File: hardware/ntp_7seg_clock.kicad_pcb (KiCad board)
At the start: 2 copper layers, 61 x 33 mm, 43 parts, among them J1 Barrel_Jack, J2 Conn_02x04_Odd_Even, J3 Conn_02x04_Odd_Even, J4 Conn_02x04_Odd_Even, J5 Conn_02x04_Odd_Even, J6 Conn_01x06_Male, Q1 NJL7302L-F3, Q2 Q_NPN_BEC, Q3 Q_NPN_BEC, SW1 SW_PUSH_SMALL_H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

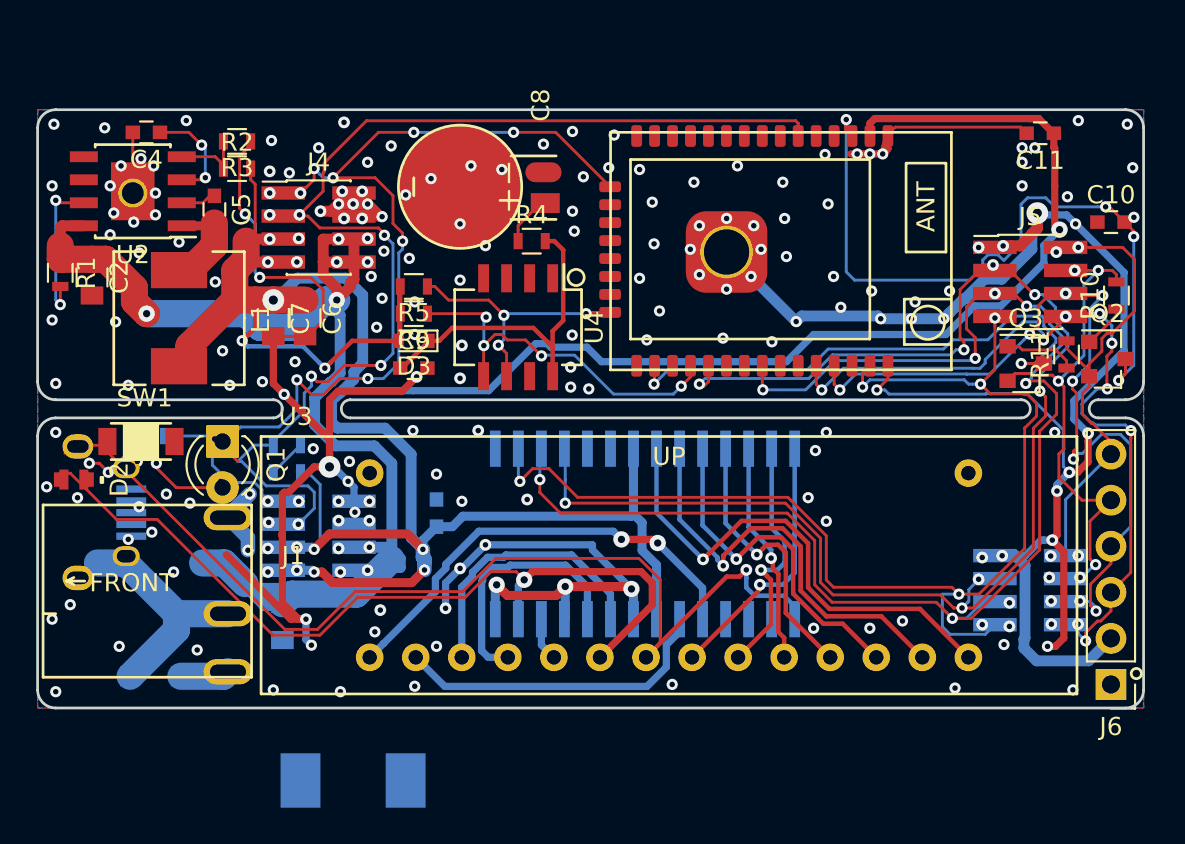
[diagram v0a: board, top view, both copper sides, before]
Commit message: Improved RTC 3V3 backup voltage handling
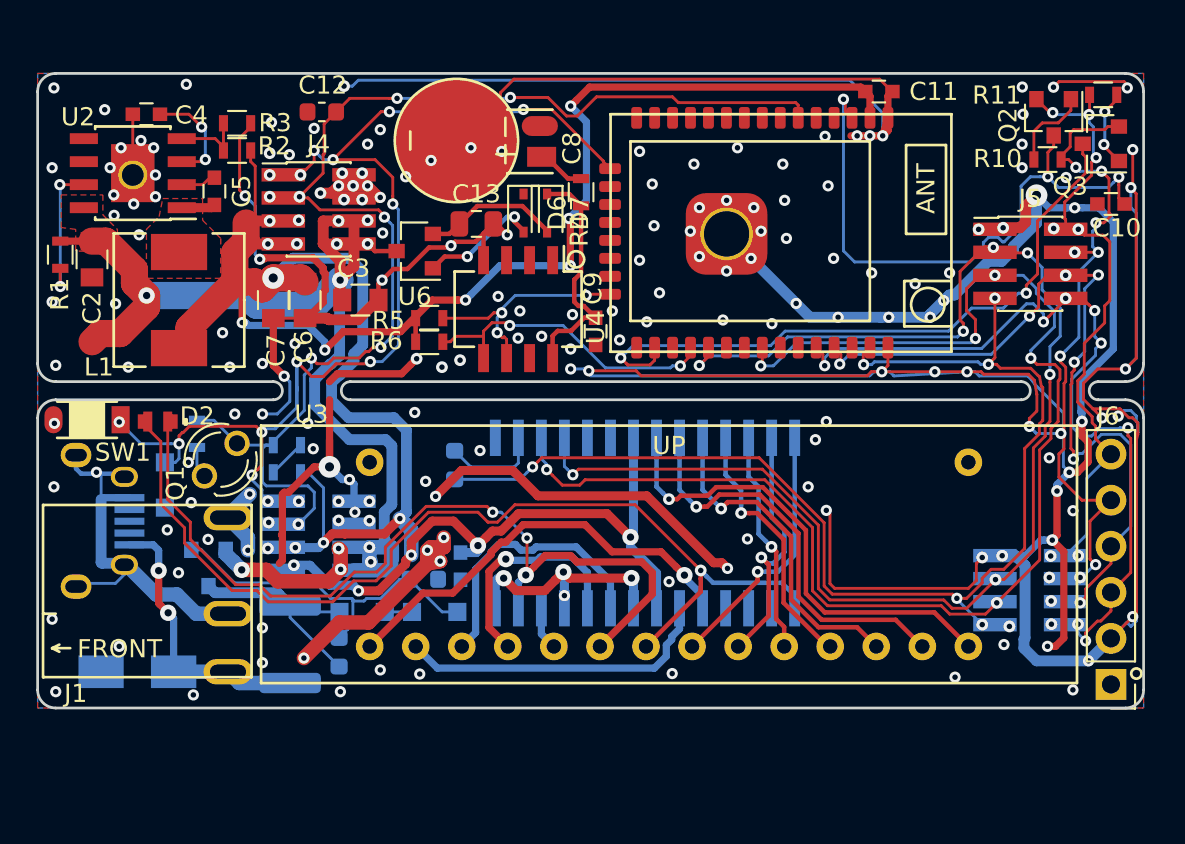
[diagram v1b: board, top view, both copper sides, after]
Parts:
- removed REF**: USB_Micro-B_Jing_A01SB141B1-067, components:USB_Micro-B_Jing_A01SB141B1-067
- added C12: 2.2u, Capacitor_SMD:C_0603_1608Metric, F.Cu at (155.7, 33.1)
- added C13: 10u/35V, Capacitor_SMD:C_0805_2012Metric, F.Cu at (164.2, 39.3)
- added D4: ESD5Z3.3T1G, Diode_SMD:D_SOD-323_HandSoldering, B.Cu at (147.0, 53.7)
- added D5: ESD5Z3.3T1G, Diode_SMD:D_SOD-323_HandSoldering, B.Cu at (157.9, 60.7)
- added D6: 1N4148W, Diode_SMD:D_SOD-323, F.Cu at (166.8, 38.7)
- added D7: 1N4148W, Diode_SMD:D_SOD-323, F.Cu at (168.1, 38.7)
- added J7: USB_B_Micro, components:USB_Micro-B_Jing_A01SB141B1-067, B.Cu at (144.8, 55.7)
- added Q4: AO3401, Package_TO_SOT_SMD:SOT-23, B.Cu at (149.4, 58.3)
- added R12: 1M, Resistor_SMD:R_0603_1608Metric, B.Cu at (156.6, 62.9)
- added R13: 22K, Resistor_SMD:R_0603_1608Metric, B.Cu at (161.3, 58.9)
- added R14: 120R, Resistor_SMD:R_0603_1608Metric, B.Cu at (163.0, 52.6)
- added U6: SE8533X2-HF, Package_TO_SOT_SMD:SOT-23, F.Cu at (160.8, 40.8)
- C3: moved to F.Cu
- D1: value D_Zener_Small -> 28V TVS; footprint Diodes_SMD:D_SOD-123F -> Diode_SMD:D_SMA
- D3: value SBD 40V 200mA -> ESD5Z3.3T1G; footprint Diodes_SMD:D_0603 -> Diode_SMD:D_SOD-323_HandSoldering; moved to B.Cu
- F1: value Polyfuse_Small -> 1A hold; footprint Capacitors_SMD:C_1812_HandSoldering -> Fuse:Fuse_1812_4532Metric
- R4: value 10R -> 1k
- moved C3 18.3 mm to (157.8, 43.5), turned to 0 degrees
- moved D3 15.0 mm to (161.9, 60.7), turned to 0 degrees
- moved R11 14.5 mm to (198.8, 32.2), turned to 180 degrees
- moved Q2 13.7 mm to (196.0, 33.4), turned to 270 degrees
- moved Q3 12.8 mm to (198.6, 34.9), turned to 180 degrees
- moved C9 10.2 mm to (170.8, 45.2), turned to 270 degrees
- moved C11 9.19 mm to (186.4, 32.0), turned to 0 degrees
- moved R10 8.41 mm to (195.7, 35.8), turned to 0 degrees
- moved F1 8.28 mm to (153.9, 62.5), turned to 90 degrees
- moved D2 5.62 mm to (146.6, 50.2)
- moved R4 3.84 mm to (170.0, 37.5), turned to 270 degrees
- moved C1 3.21 mm to (163.3, 58.2), turned to 270 degrees
- moved SW1 3.21 mm to (142.7, 50.1), turned to 180 degrees
- moved C8 2.56 mm to (167.8, 34.7)
- moved R7 2.54 mm to (148.8, 50.9), turned to 90 degrees
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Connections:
- C9 pad 1: Net-(C9-Pad1) -> /3V3_RTC
- D3 pad 1: Net-(C9-Pad1) -> Net-(D3-Pad1)
- D3 pad 2: +3V3 -> Net-(D3-Pad2)
- F1 pad 2: /VIN -> Net-(D5-Pad2)
- J1 pad 2: GND -> Net-(J1-Pad2)
- J1 pad 3: GND -> Net-(J1-Pad3)
- R4 pad 2: Net-(C9-Pad1) -> /3V3_RTC
- U1 pad 2: E_LED_DIO -> Net-(R14-Pad1)
- U4 pad 8: Net-(C9-Pad1) -> /3V3_RTC
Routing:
- net GND: track 198.3 -> 390.9 mm, vias 175 -> 179
- net Net-(J1-Pad3): track 0.00 -> 22.1 mm, vias 0 -> 1
- net +3V3: track 168.4 -> 146.8 mm, vias 16 -> 20
- net Net-(D3-Pad2): track 0.00 -> 19.5 mm
- net Net-(C9-Pad1): track 18.2 -> 0.00 mm
- net /3V3_RTC: track 0.00 -> 13.1 mm
- net Net-(D5-Pad2): track 0.00 -> 12.4 mm
- net DTR: track 28.6 -> 37.5 mm, vias 6 -> 9
- net RTS: track 26.0 -> 34.1 mm, vias 4 -> 7
- net /3V3+: track 0.00 -> 7.57 mm
- net E_GPIO0: track 29.4 -> 36.4 mm
- net E_EN: track 39.9 -> 33.1 mm, vias 4 -> 3
- net Net-(D6-Pad2): track 0.00 -> 6.72 mm, vias 0 -> 2
- net E_BUTTON: track 58.8 -> 65.2 mm, vias 13 -> 15
- net Net-(R14-Pad1): track 0.00 -> 5.36 mm
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- added copper zone on F.Cu, net /VIN
- added copper zone on F.Cu, net Net-(C5-Pad2)
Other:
- board size 61 x 33 mm -> 61 x 35 mm
- board text added: "draw shield line at the every edge of the board"

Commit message: Ooops reverse protection FET is reversed; and others
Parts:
- C8: value EDLC -> ML621; footprint components:BAT_6814_LAY -> components:BAT_MS621T_LAY
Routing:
- net GND: track 390.9 -> 401.1 mm, vias 179 -> 185
- net +3V3: track 146.8 -> 145.0 mm
- net Net-(C8-Pad1): track 2.67 -> 4.11 mm

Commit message: Modified to use Li-ion rechargable battery
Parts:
- removed C13: 10u/35V, Capacitor_SMD:C_0805_2012Metric
- removed D5: ESD5Z3.3T1G, Diode_SMD:D_SOD-323_HandSoldering
- removed D6: 1N4148W, Diode_SMD:D_SOD-323
- removed U6: SE8533X2-HF, Package_TO_SOT_SMD:SOT-23
- added Q5: Q_NPN_BEC, Package_TO_SOT_SMD:SOT-23, F.Cu at (162.5, 40.2)
- added Q6: AO3401, Package_TO_SOT_SMD:SOT-23, F.Cu at (161.2, 43.1)
- added R15: 10k, Resistor_SMD:R_0603_1608Metric, F.Cu at (165.7, 39.0)
- added R16: 10k, Resistor_SMD:R_0603_1608Metric, F.Cu at (160.3, 40.0)
- D7: value 1N4148W -> SBD
- moved R12 2.81 mm to (158.2, 60.6), turned to 0 degrees
- moved R5 1.00 mm to (161.7, 45.5)
- moved R6 1.00 mm to (161.7, 46.8)
- turned Q4 to 180 degrees
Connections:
- D3 pad 1: Net-(D3-Pad1) -> /VIN
- D7 pad 2: /3V3+ -> Net-(D7-Pad2)
- F1 pad 2: Net-(D5-Pad2) -> Net-(F1-Pad2)
- Q4 pad 2: /VIN -> Net-(F1-Pad2)
- Q4 pad 3: Net-(D5-Pad2) -> /VIN
- R12 pad 2: Net-(D5-Pad2) -> /VIN
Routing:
- net +3V3: track 145.0 -> 160.8 mm
- net Net-(D5-Pad2): track 12.4 -> 0.00 mm
- net /3V3+: track 7.57 -> 0.00 mm
- net Net-(D7-Pad2): track 0.00 -> 7.29 mm, vias 0 -> 2
- net Net-(D6-Pad2): track 6.72 -> 0.00 mm, vias 2 -> 0
- net /VIN: track 70.5 -> 76.7 mm
- net GND: track 401.1 -> 395.4 mm, vias 185 -> 180
- net Net-(Q5-Pad3): track 0.00 -> 4.10 mm
- net Net-(F1-Pad2): track 0.00 -> 3.96 mm
- net Net-(D2-Pad1): track 47.3 -> 49.1 mm
- net Net-(D2-Pad2): track 54.0 -> 55.7 mm
- net Net-(Q5-Pad1): track 0.00 -> 1.55 mm
- net Net-(D3-Pad1): track 1.50 -> 0.00 mm
- net Net-(D3-Pad2): track 19.5 -> 18.1 mm

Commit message: Layout fix
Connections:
- J1 pad 2: Net-(J1-Pad2) -> GND
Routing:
- net GND: track 395.4 -> 400.7 mm, vias 180 -> 182
- net Net-(J1-Pad2): track 4.05 -> 0.00 mm, vias 2 -> 0
- net E_BUTTON: track 65.2 -> 65.8 mm
